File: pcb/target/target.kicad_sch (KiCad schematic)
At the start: 0 parts

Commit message: Target: Added stm32 and connectors to schematic
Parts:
- added C1: 100nF, Capacitor_SMD:C_0603_1608Metric, symbol Device:C
- added C2: 4.7uF, Capacitor_SMD:C_0603_1608Metric, symbol Device:C
- added C3: 0.1uF, symbol Device:C
- added J1, J2: Conn_02x03_Counter_Clockwise, symbol Connector_Generic:Conn_02x03_Counter_Clockwise
- added R1: 10kR, symbol Device:R
- added SW1, SW2: HX TS3315A-H 250GF, lcsc:SW-SMD_4P-L3.4-W3.4-P2.00-LS4.0_TS3315A160GF, symbol lcsc:HXTS3315A-H250GF
- added U1: STM32C011F4P6TR, lcsc:TSSOP-20_L6.5-W4.4-P0.65-LS6.4-BL, symbol lcsc:STM32C011F4P6TR
- added U2: SC7A20HTR, lcsc:LGA-12_L2.0-W2.0-P0.50-TL, symbol lcsc:SC7A20HTR
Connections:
- new net +3V3: C1.1, C2.1, J1.1 (Pin_1), J2.1 (Pin_1), SW1.1 (A), U1.4 (VDD/VDDA)
- new net A: J1.5 (Pin_5), J2.5 (Pin_5)
- new net B: J1.4 (Pin_4), J2.4 (Pin_4)
- new net BOOT0: R1.1, SW1.3 (C), U1.18 (PA13), U1.19 (PA14-BOOT0)
- new net DBG_LED: U1.14 (PA7)
- new net DE: U1.17 (PA12[PA10])
- new net GND: C1.2, C2.2, C3.2, J1.6 (Pin_6), J2.6 (Pin_6), R1.2, SW1.5 (GND), SW2.3 (C), SW2.5 (GND), U1.5 (VSS/VSSA)
- new net INT_IN: J1.3 (Pin_3), J2.3 (Pin_3), U1.9 (PA2)
- new net INT_OUT: J1.2 (Pin_2), J2.2 (Pin_2), U1.10 (PA3)
- new net LED_G1: U1.12 (PA5)
- new net LED_G2: U1.20 (PB6)
- new net NRST: C3.1, SW2.1 (A), U1.6 (PF2-NRST)
- new net RX: U1.8 (PA1)
- new net SCL: U1.1 (PB7)
- new net SDA: U1.2 (PC14-OSCX_IN)
- new net TX: U1.7 (PA0)
- no-connect marks 0 -> 9
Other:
- added sheet LEDs (leds.kicad_sch)
- note added: "max 20mA draw per pin"

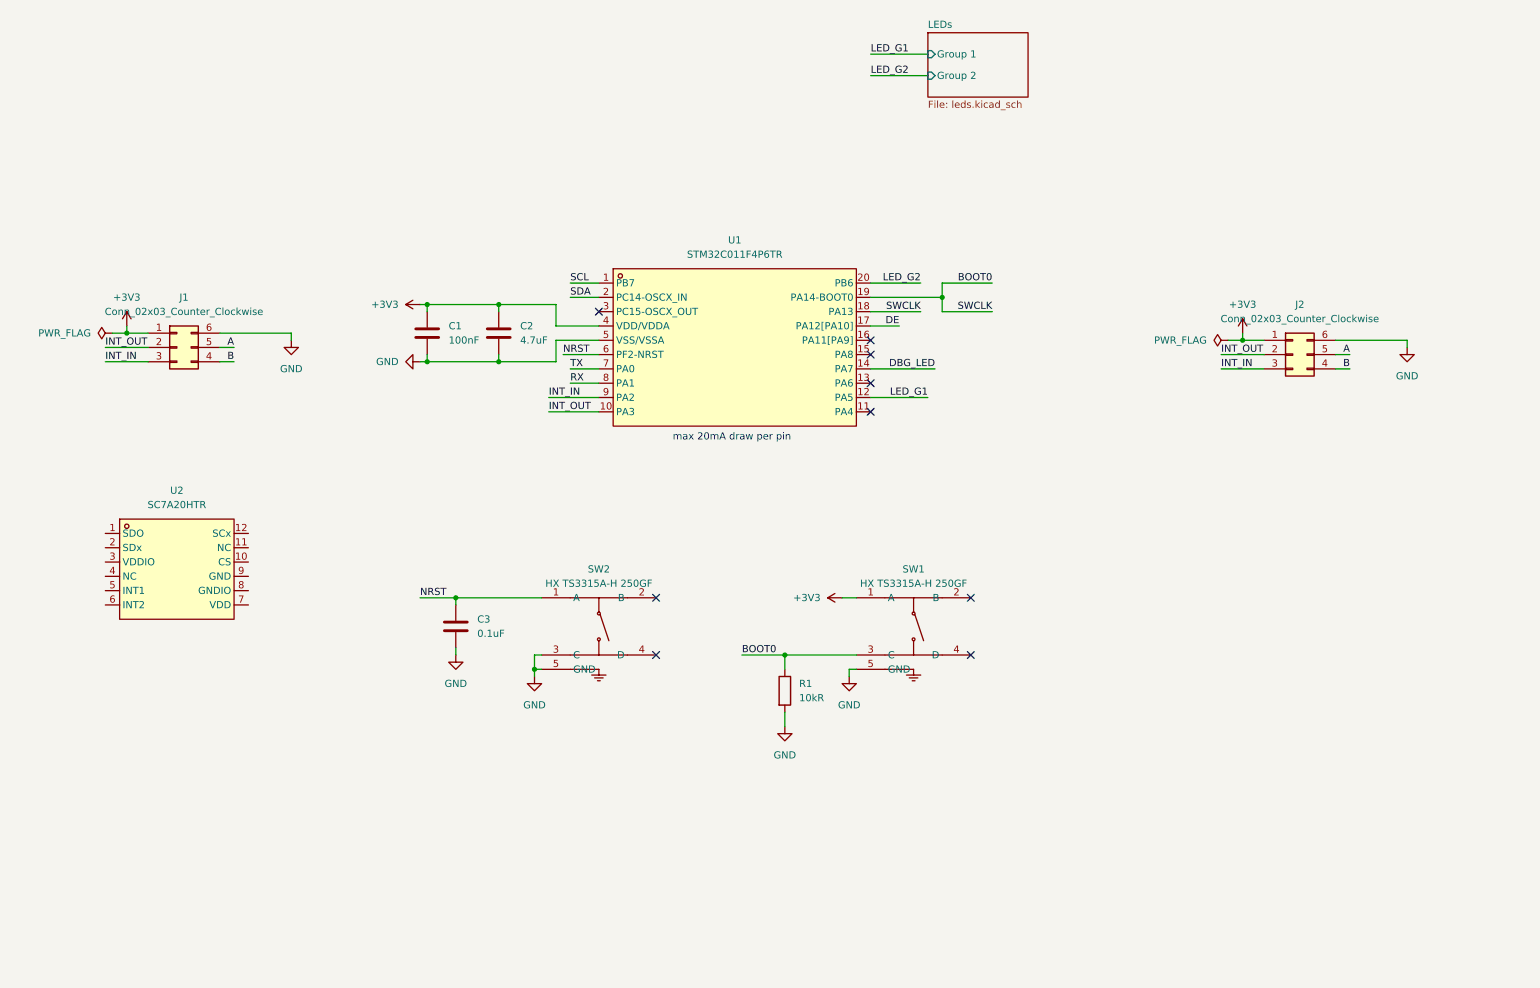
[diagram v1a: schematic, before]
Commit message: First iteration of target schematic
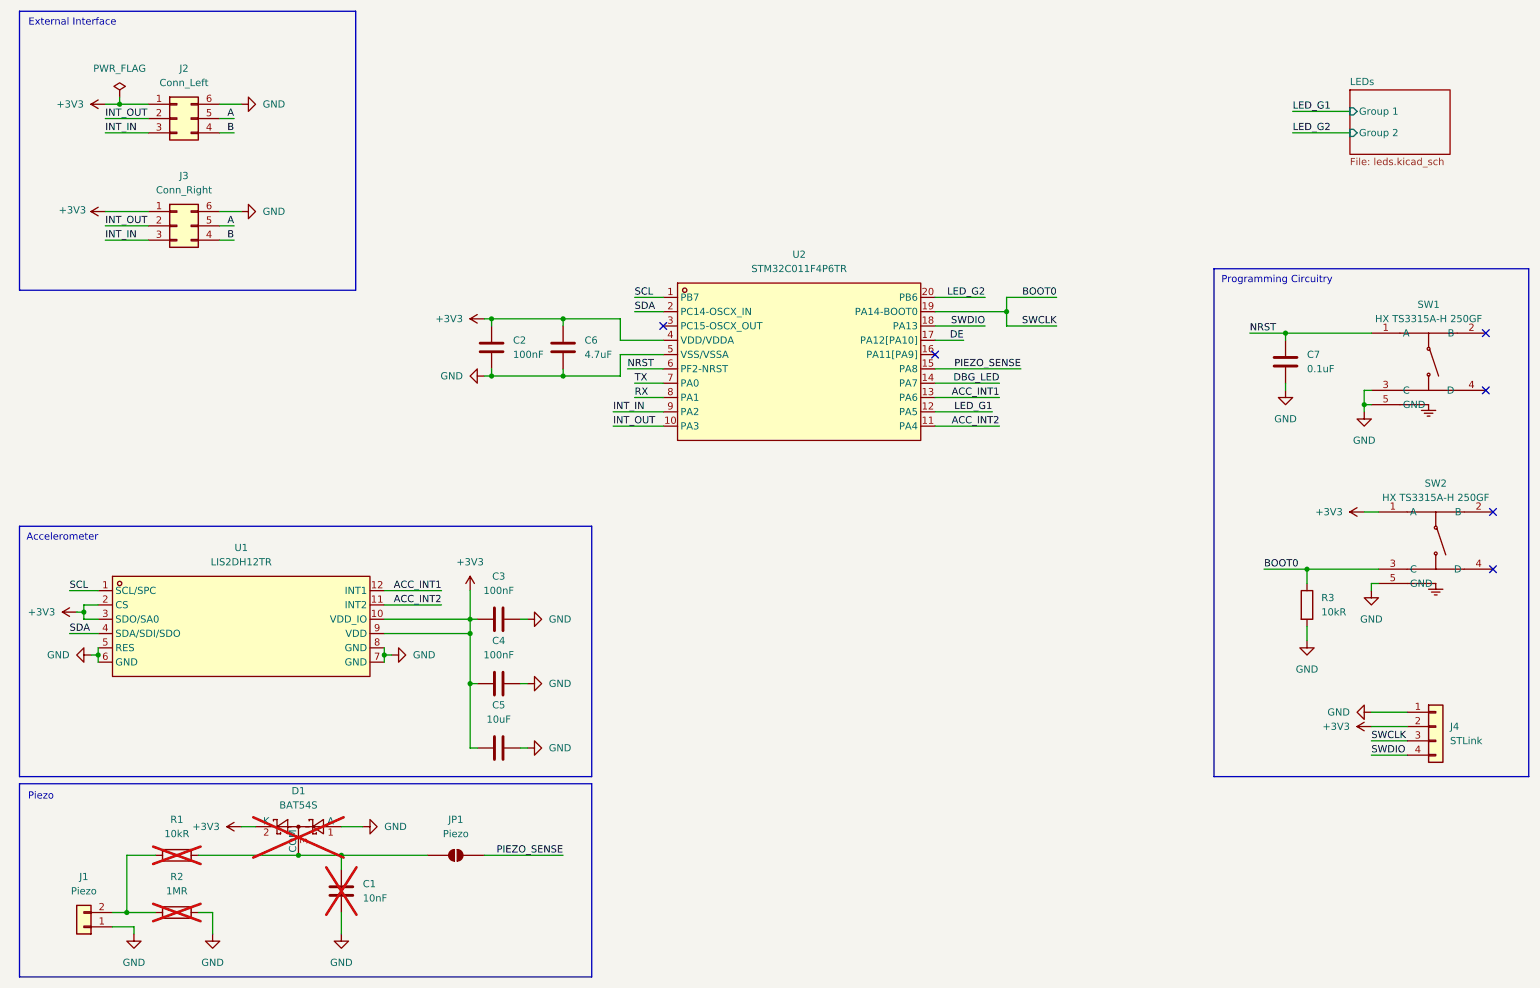
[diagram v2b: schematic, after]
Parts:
- removed U2: SC7A20HTR, lcsc:LGA-12_L2.0-W2.0-P0.50-TL, symbol lcsc:SC7A20HTR
- added C1: 10nF, symbol Device:C
- added C3, C4: 100nF, symbol Device:C
- added C5: 10uF, symbol Device:C
- added D1: BAT54S, Package_TO_SOT_SMD:SOT-23, symbol Diode:BAT54S
- added J1: Piezo, Connector_PinHeader_1.27mm:PinHeader_1x02_P1.27mm_Vertical, symbol Connector_Generic:Conn_01x02
- added J4: STLink, Connector_PinSocket_2.54mm:PinSocket_1x04_P2.54mm_Vertical, symbol Connector_Generic:Conn_01x04
- added JP1: Piezo, Jumper:SolderJumper-2_P1.3mm_Open_RoundedPad1.0x1.5mm, symbol Jumper:SolderJumper_2_Open
- added R1: 10kR, Resistor_SMD:R_0603_1608Metric, symbol Device:R
- added R2: 1MR, Resistor_SMD:R_0603_1608Metric, symbol Device:R
- added U1: LIS2DH12TR, lcsc:LGA-12_L2.0-W2.0-P0.50-BL, symbol lcsc:LIS2DH12TR
- J2: renamed from J1; value Conn_02x03_Counter_Clockwise -> Conn_Left
- J3: renamed from J2; value Conn_02x03_Counter_Clockwise -> Conn_Right
- renumbered C1 to C2, C2 to C6, C3 to C7, R1 to R3, SW2 to SW1, SW1 to SW2, U1 to U2
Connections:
- net +3V3: now also C3.1, C4.2, C5.2, D1.2 (K), J4.2 (Pin_2), U1.10 (VDD_IO), U1.2 (CS), U1.3 (SDO/SA0), U1.9 (VDD)
- net BOOT0: now also J4.3 (Pin_3); no longer U2.18 (PA13)
- net GND: now also C1.2, C3.2, C4.1, C5.1, D1.1 (A), J1.1 (Pin_1), J4.1 (Pin_1), R2.2, U1.5 (RES), U1.6 (GND), U1.7 (GND), U1.8 (GND)
- net SCL: now also U1.1 (SCL/SPC)
- net SDA: now also U1.4 (SDA/SDI/SDO)
- net ACC_INT2: now reaches U2.11 (PA4)
- net ACC_INT2: now also U1.11 (INT2)
- net ACC_INT1: now reaches U2.13 (PA6)
- net ACC_INT1: now also U1.12 (INT1)
- net PIEZO_SENSE: now reaches U2.15 (PA8)
- net PIEZO_SENSE: now also JP1.2 (B)
- new net: J1.2 (Pin_2), R1.1, R2.1
- new net: C1.1, D1.3 (COM), JP1.1 (A), R1.2
- new net SWDIO: J4.4 (Pin_4), U2.18 (PA13)
- no-connect marks 9 -> 6
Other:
- note added: "Accelerometer"
- note added: "External Interface"
- note added: "Piezo"
- note added: "Programming Circuitry"
- note removed: "max 20mA draw per pin"
- title: (none) -> BlitzPong-Target
- moved on the sheet: C2, C6, C7, J2, J3, R3, SW1, SW2, U2

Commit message: Started controller schematic
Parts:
- added U3: SP3485EN-L/TR, lcsc:SOIC-8_L5.0-W4.0-P1.27-LS6.0-BL, symbol lcsc:SP3485EN-L_TR
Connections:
- net +3V3: now also U3.8 (VCC)
- net A: now also U3.6 (A)
- net B: now also U3.7 (B)
- net DE: now also U3.3 (DE)
- net GND: now also U3.5 (GND)
- net RX: now also U3.1 (RO)
- net TX: now also U3.4 (DI)
- net RE: now reaches U2.16 (PA11[PA9])
- net RE: now also U3.2 (~{RE})
- no-connect marks 6 -> 5
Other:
- note added: "RS-485"
